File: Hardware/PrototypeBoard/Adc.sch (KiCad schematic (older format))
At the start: 25 parts

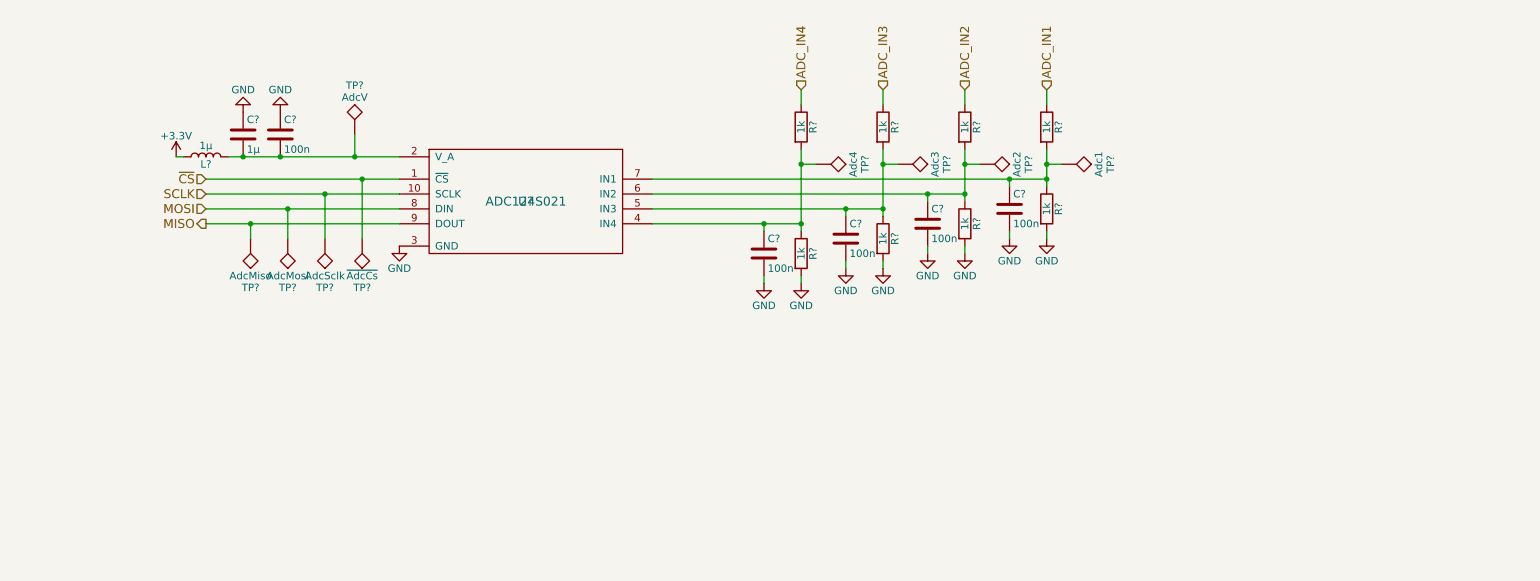
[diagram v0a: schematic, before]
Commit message: Fixed all ERC errors. Added power consumption estimation and other comments. Added links to datasheets. Dimensioned low pass and voltage dividers. Added TVS diodes for protection of voltage rails and ADC inputs. Added fuses. Added Testpoints. Added DC-link capacitors.
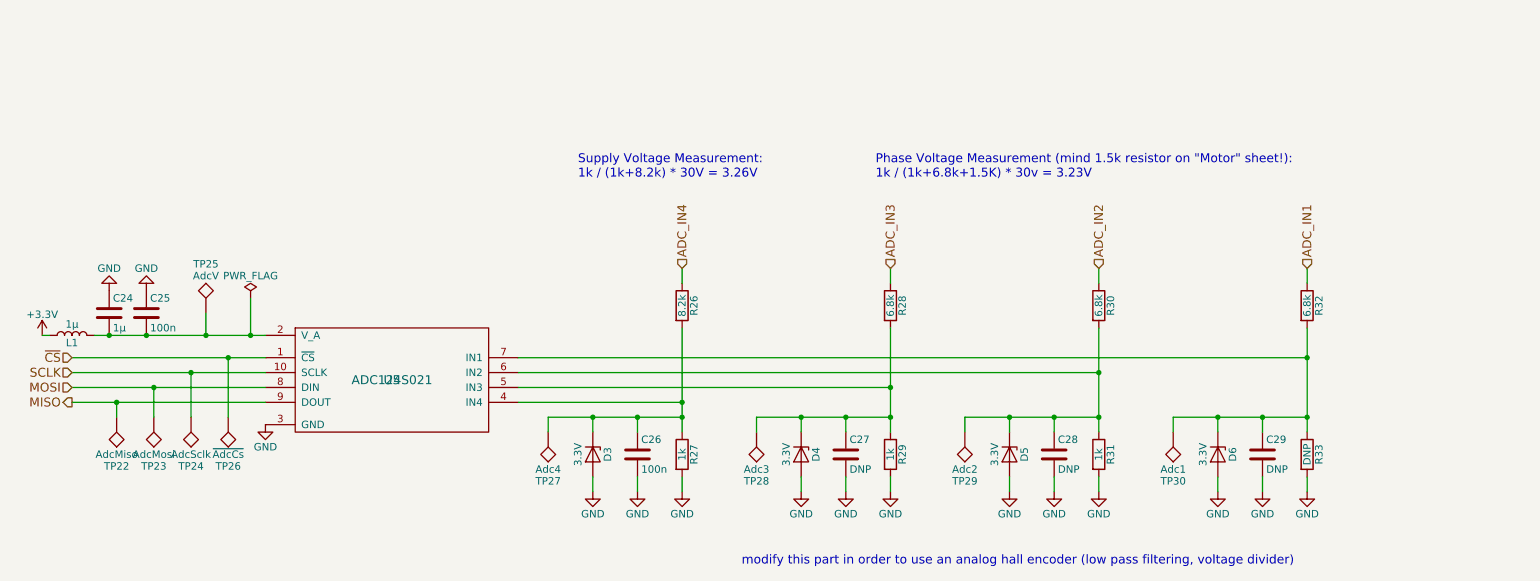
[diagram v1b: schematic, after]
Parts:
- added D3, D4, D5, D6: 3.3V, symbol D_Zener
- C27, C28, C29: renamed from C?; value 100n -> DNP
- R26: renamed from R?; value 1k -> 8.2k
- R28, R30, R32: renamed from R?; value 1k -> 6.8k
- R33: renamed from R?; value 1k -> DNP
- gave numbers to parts that had none: 17
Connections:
- net GND: now also D3.2 (A), D4.2 (A), D5.2 (A), D6.2 (A)
- net at C26.1, R26.2, R27.1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: now also D3.1 (K)
- net at C27.1, R28.2, R29.1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: now also D4.1 (K)
- net at C28.1, R30.2, R31.1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: now also D5.1 (K)
- net at C29.1, R32.2, R33.1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: now also D6.1 (K)
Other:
- note added: "Phase Voltage Measurement (mind 1.5k resistor on "Motor" sheet!):\n1k / (1k+6.8k+1.5K) * 30v = 3.23V"
- note added: "Supply Voltage Measurement:\n1k / (1k+8.2k) * 30V = 3.26V"
- note added: "modify this part in order to use an analog hall encoder (low pass filtering, voltage divider)"
- moved on the sheet: C24, C25, C26, C27, C28, C29, L1, R26, R27, R28, R29, R30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
